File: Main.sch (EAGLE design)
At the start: 11 parts, among them U2 LM 1084 IT5,0, U3 LM 1084 IT3,3, X1 12V

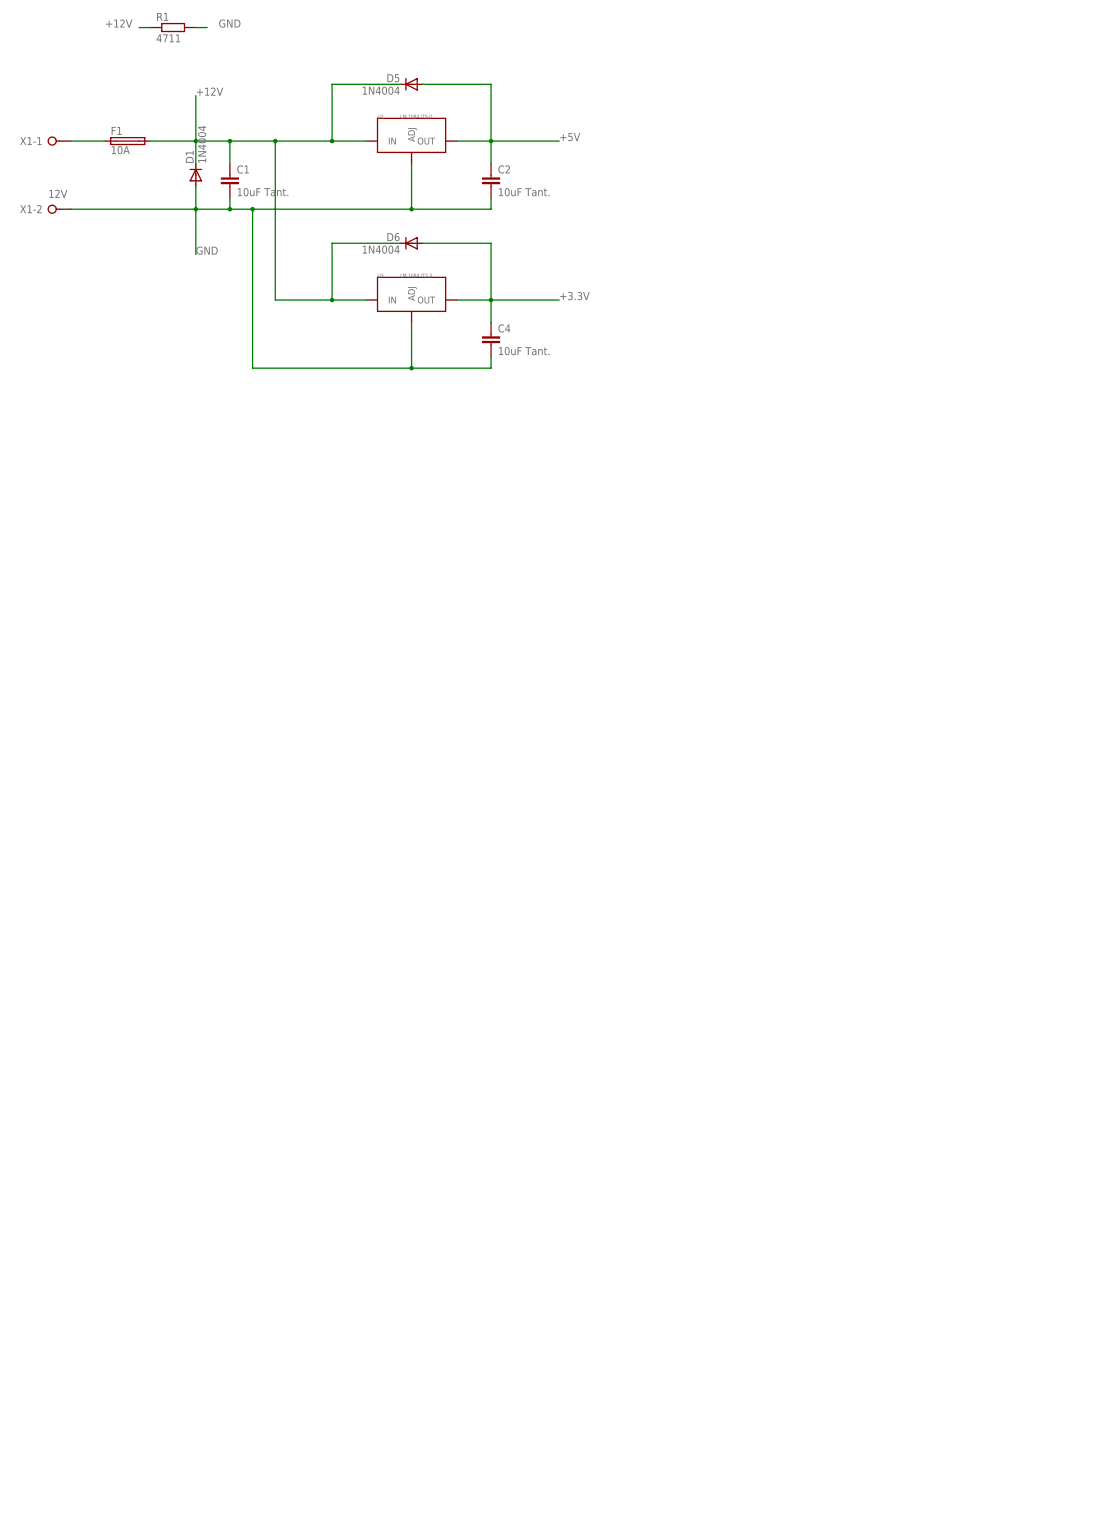
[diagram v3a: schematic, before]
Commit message: added first motor driver
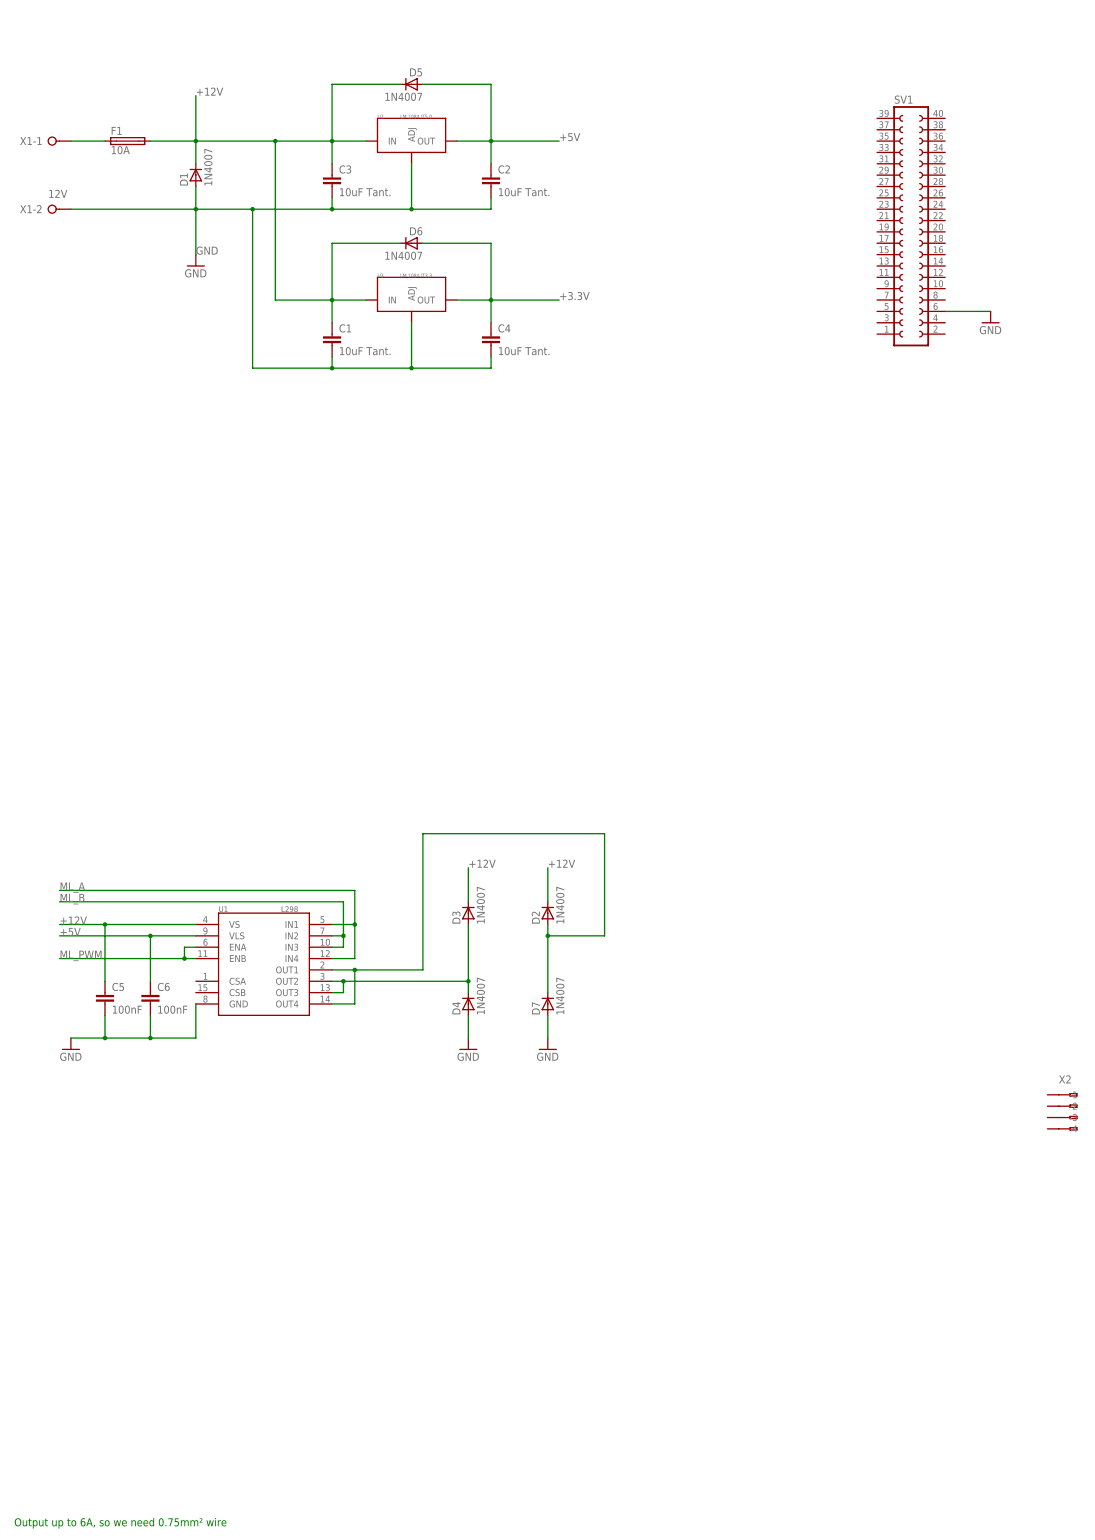
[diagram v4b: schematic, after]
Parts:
- removed R1: 4711, resistor:R-EU_0617/22
- added C3: 10uF Tant., rcl:C-EU025-040X050
- added C5, C6: 100nF, rcl:C-EUC0805
- added D2, D3, D4, D7: 1N4007, semicon-smd-ipc:D-MLL-41
- added SV1: (no value), con-lsta:FE20-2
- added U1: L298, SparkFun-PowerIC:L298
- added X2: (no value), con-wago255:233-504
- D1, D5, D6: value 1N4004 -> 1N4007; device diode:1N4004 -> semicon-smd-ipc:D-MLL-41
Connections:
- new net ML_A: U1.IN1, U1.IN4
- new net ML_B: U1.IN2, U1.IN3
- new net ML_PWM: U1.ENA, U1.ENB
- new net N$4: D3.A, D4.C, U1.OUT2, U1.OUT3
- new net N$5: D2.A, D7.C, U1.OUT1, U1.OUT4
- net +12V: now also C3.1, C5.1, D2.C, D3.C, U1.VS; no longer R1.1
- net +5V: now also C6.1, U1.VLS
- net GND: now also C3.2, C5.2, C6.2, D4.A, D7.A, SV1.6, U1.GND; no longer R1.2
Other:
- note added: "Output up to 6A, so we need 0.75mm² wire"
- moved on the sheet: C1

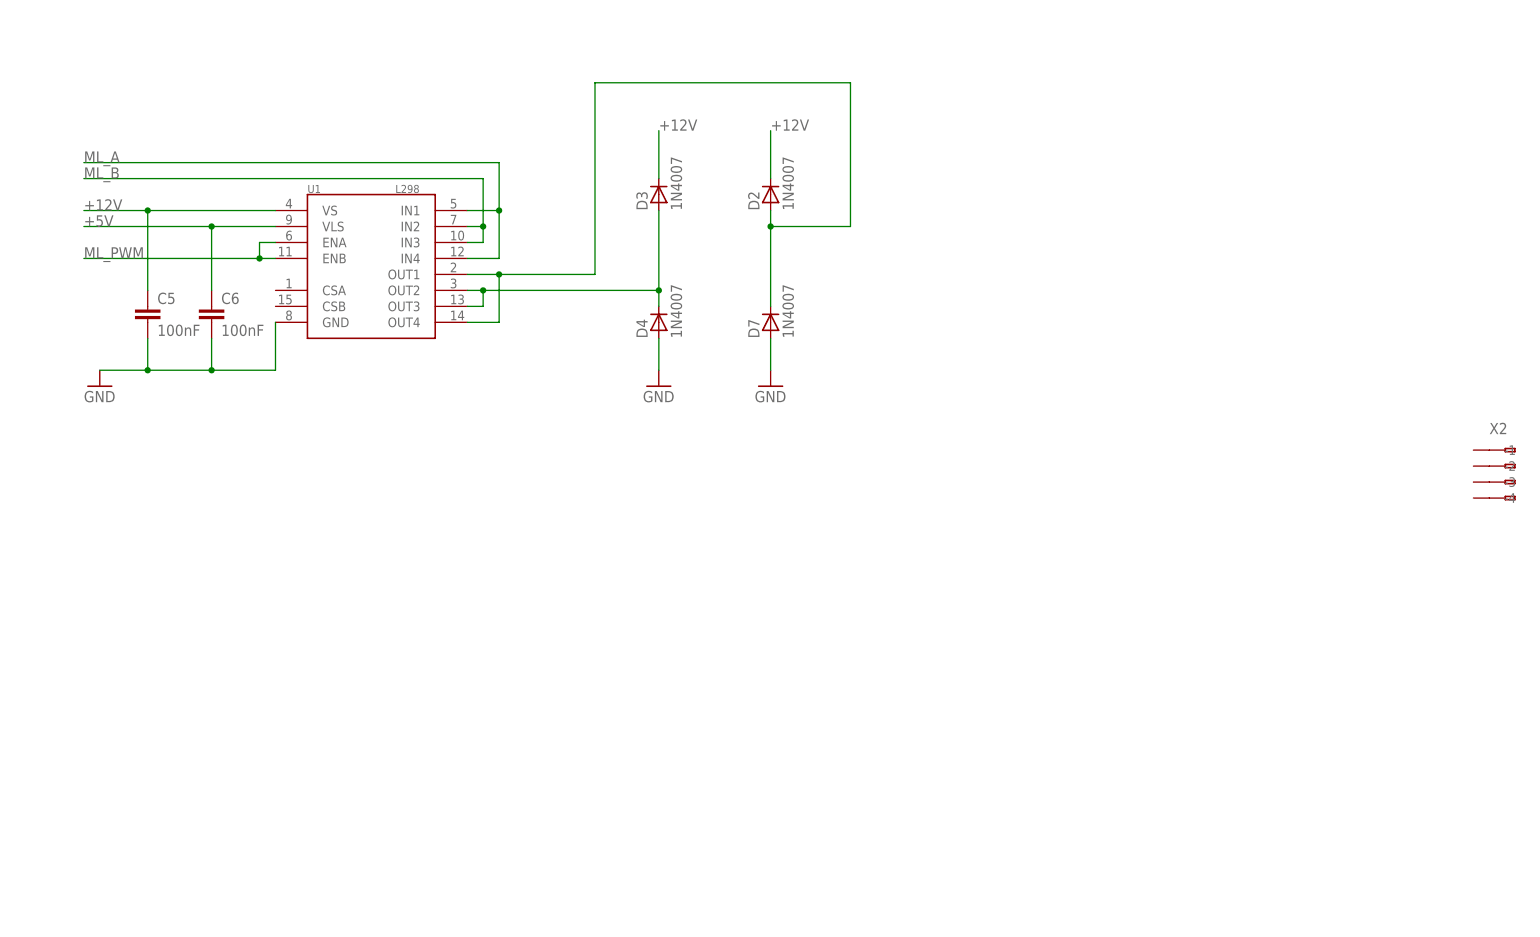
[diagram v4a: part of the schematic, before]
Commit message: added second motor driver and fixed protction diodes
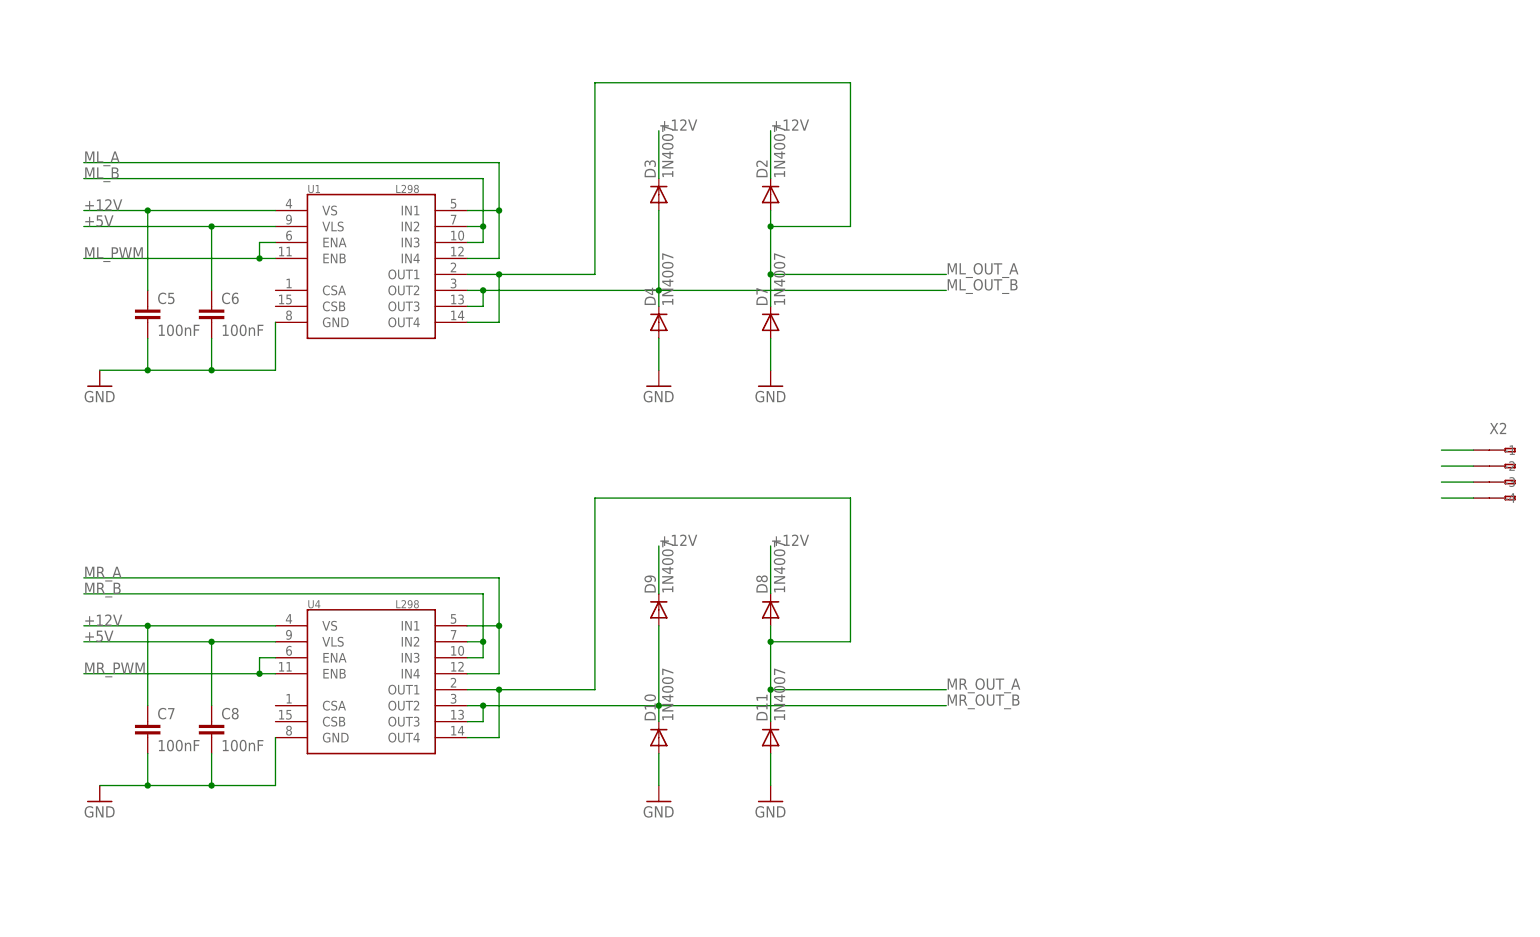
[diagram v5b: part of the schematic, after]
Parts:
- added C7, C8: 100nF, rcl:C-EUC0805
- added D10, D11, D8, D9: 1N4007, diode:P600
- added U4: L298, SparkFun-PowerIC:L298
- D2, D3, D4, D7: device semicon-smd-ipc:D-MLL-41 -> diode:P600
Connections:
- removed net N$4: D3.A, D4.C, U1.OUT2, U1.OUT3
- removed net N$5: D2.A, D7.C, U1.OUT1, U1.OUT4
- new net ML_OUT_A: D2.A, D7.C, U1.OUT1, U1.OUT4, X2.-1
- new net ML_OUT_B: D3.A, D4.C, U1.OUT2, U1.OUT3, X2.-2
- new net MR_A: U4.IN1, U4.IN4
- new net MR_B: U4.IN2, U4.IN3
- new net MR_OUT_A: D11.C, D8.A, U4.OUT1, U4.OUT4, X2.-3
- new net MR_OUT_B: D10.C, D9.A, U4.OUT2, U4.OUT3, X2.-4
- new net MR_PWM: U4.ENA, U4.ENB
- net +12V: now also C7.1, D8.C, D9.C, U4.VS
- net +5V: now also C8.1, U4.VLS
- net GND: now also C7.2, C8.2, D10.A, D11.A, U4.GND

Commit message: some routing experiments
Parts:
- U2: value LM 1084 IT5,0 -> LM 1085 IT5,0; device PP_PowerIC:LM1084TO-263-3 -> linear-technology-3:LT1085IT-V
- U3: value LM 1084 IT3,3 -> LM 1085 IT3,3; device PP_PowerIC:LM1084TO-263-3 -> linear-technology-3:LT1085IT-V
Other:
- moved on the sheet: U2, U3
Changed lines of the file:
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@@
 <layer number="223" name="223bmp" color="24" fill="1" visible="no" active="no"/>
 <layer number="224" name="224bmp" color="25" fill="1" visible="no" active="no"/>
+<layer number="231" name="Eagle3D_PG1" color="14" fill="1" visible="yes" active="yes"/>
+<layer number="232" name="Eagle3D_PG2" color="14" fill="2" visible="yes" active="yes"/>
+<layer number="233" name="Eagle3D_PG3" color="14" fill="4" visible="yes" active="yes"/>
 <layer number="250" name="Descript" color="3" fill="1" visible="no" active="no"/>
 <layer number="251" name="SMDround" color="12" fill="11" visible="no" active="no"/>
@@
 </classes>
 <parts>
-<part name="U2" library="PP_PowerIC" deviceset="LM1084" device="TO-263-3" value="LM 1084 IT5,0"/>
+<part name="U2" library="linear-technology-3" deviceset="LT1085*" device="T-V" technology="I" value="LM 1085 IT5,0"/>
 <part name="D5" library="semicon-smd-ipc" deviceset="D-" device="MLL-41" value="1N4007"/>
 <part name="C1" library="rcl" deviceset="C-EU" device="025-040X050" value="10uF Tant."/>
 <part name="C2" library="rcl" deviceset="C-EU" device="025-040X050" value="10uF Tant."/>
 <part name="X1" library="con-wago-508" deviceset="W237-02P" device="" value="12V"/>
-<part name="U3" library="PP_PowerIC" deviceset="LM1084" device="TO-263-3" value="LM 1084 IT3,3"/>
+<part name="U3" library="linear-technology-3" deviceset="LT1085*" device="T-V" technology="I" value="LM 1085 IT3,3"/>
 <part name="D6" library="semicon-smd-ipc" deviceset="D-" device="MLL-41" value="1N4007"/>
 <part name="C4" library="rcl" deviceset="C-EU" device="025-040X050" value="10uF Tant."/>
@@
 <label x="-378.46" y="340.36" size="1.778" layer="95"/>
 <pinref part="U2" gate="G$1" pin="OUT"/>
-<wire x1="-393.7" y1="340.36" x2="-401.32" y2="340.36" width="0.1524" layer="91"/>
+<wire x1="-393.7" y1="340.36" x2="-403.86" y2="340.36" width="0.1524" layer="91"/>
 </segment>
 <segment>
@@
 <label x="-378.46" y="304.8" size="1.778" layer="95"/>
 <pinref part="U3" gate="G$1" pin="OUT"/>
-<wire x1="-401.32" y1="304.8" x2="-393.7" y2="304.8" width="0.1524" layer="91"/>
+<wire x1="-403.86" y1="304.8" x2="-393.7" y2="304.8" width="0.1524" layer="91"/>
 </segment>
 </net>
 <net name="+12V" class="0">
 <segment>
-<wire x1="-429.26" y1="304.8" x2="-421.64" y2="304.8" width="0.1524" layer="91"/>
+<wire x1="-429.26" y1="304.8" x2="-419.1" y2="304.8" width="0.1524" layer="91"/>
 <junction x="-429.26" y="304.8"/>
 <wire x1="-429.26" y1="304.8" x2="-429.26" y2="317.5" width="0.1524" layer="91"/>
@@
 <pinref part="U3" gate="G$1" pin="IN"/>
 <wire x1="-429.26" y1="304.8" x2="-441.96" y2="304.8" width="0.1524" layer="91"/>
-<wire x1="-429.26" y1="340.36" x2="-421.64" y2="340.36" width="0.1524" layer="91"/>
+<wire x1="-429.26" y1="340.36" x2="-419.1" y2="340.36" width="0.1524" layer="91"/>
 <junction x="-429.26" y="340.36"/>
 <wire x1="-429.26" y1="340.36" x2="-429.26" y2="353.06" width="0.1524" layer="91"/>
@@
 <wire x1="-411.48" y1="289.56" x2="-393.7" y2="289.56" width="0.1524" layer="91"/>
 <pinref part="U3" gate="G$1" pin="ADJ"/>
-<wire x1="-411.48" y1="299.72" x2="-411.48" y2="289.56" width="0.1524" layer="91"/>
+<wire x1="-411.48" y1="297.18" x2="-411.48" y2="289.56" width="0.1524" layer="91"/>
 <junction x="-411.48" y="289.56"/>
 <wire x1="-411.48" y1="325.12" x2="-393.7" y2="325.12" width="0.1524" layer="91"/>
 <pinref part="U2" gate="G$1" pin="ADJ"/>
-<wire x1="-411.48" y1="335.28" x2="-411.48" y2="325.12" width="0.1524" layer="91"/>
+<wire x1="-411.48" y1="332.74" x2="-411.48" y2="325.12" width="0.1524" layer="91"/>
 <junction x="-411.48" y="325.12"/>
 <wire x1="-447.04" y1="325.12" x2="-429.26" y2="325.12" width="0.1524" layer="91"/>
